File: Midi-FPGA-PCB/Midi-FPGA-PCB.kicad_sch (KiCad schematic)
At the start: 4 parts

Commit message: Arranged and documented
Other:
- title: (none) -> Midi FPGA
- moved on the sheet: H1, H2, H3, H4
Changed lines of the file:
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@@
 (kicad_sch (version 20230121) (generator eeschema)
   (paper "A4")
-  (rectangle (start 20.32 16.51) (end 72.39 45.72)
+  (title_block
+    (title "Midi FPGA")
+    (date "2023-11-07")
+    (rev "1.0")
+  )
+  (wire (pts (xy 20.32 22.86) (xy 20.32 24.13))
+    (stroke (width 0) (type default))
+  )
+  (wire (pts (xy 45.72 38.1) (xy 45.72 36.83))
+    (stroke (width 0) (type default))
+  )
+  (wire (pts (xy 20.32 38.1) (xy 20.32 36.83))
+    (stroke (width 0) (type default))
+  )
+  (wire (pts (xy 45.72 22.86) (xy 45.72 24.13))
+    (stroke (width 0) (type default))
+  )
+  (rectangle (start 15.24 15.24) (end 67.31 44.45)
     (stroke (width 0) (type default))
     (fill (type none))
   )
-  (symbol (lib_id "Mechanical:MountingHole_Pad") (at 50.8 35.56 0) (unit 1)
+  (symbol (lib_id "Mechanical:MountingHole_Pad") (at 45.72 34.29 0) (unit 1)
     (in_bom yes) (on_board yes) (dnp no) (fields_autoplaced)
-    (property "Reference" "H4" (at 53.34 33.02 0)
+    (property "Reference" "H4" (at 48.26 31.75 0)
       (effects (font (size 1.27 1.27)) (justify left))
     )
-    (property "Value" "MountingHole_Pad" (at 53.34 35.56 0)
+    (property "Value" "MountingHole_Pad" (at 48.26 34.29 0)
       (effects (font (size 1.27 1.27)) (justify left))
     )
-    (property "Footprint" "MountingHole:MountingHole_2.2mm_M2_DIN965_Pad" (at 50.8 35.56 0)
+    (property "Footprint" "MountingHole:MountingHole_2.2mm_M2_DIN965_Pad" (at 45.72 34.29 0)
       (effects (font (size 1.27 1.27)) hide)
     )
-    (property "Datasheet" "~" (at 50.8 35.56 0)
+    (property "Datasheet" "~" (at 45.72 34.29 0)
       (effects (font (size 1.27 1.27)) hide)
     )
@@
     )
   )
-  (symbol (lib_id "Mechanical:MountingHole_Pad") (at 50.8 22.86 0) (unit 1)
+  (symbol (lib_id "Mechanical:MountingHole_Pad") (at 45.72 20.32 0) (unit 1)
     (in_bom yes) (on_board yes) (dnp no) (fields_autoplaced)
-    (property "Reference" "H2" (at 53.34 20.32 0)
+    (property "Reference" "H2" (at 48.26 17.78 0)
       (effects (font (size 1.27 1.27)) (justify left))
     )
-    (property "Value" "MountingHole_Pad" (at 53.34 22.86 0)
+    (property "Value" "MountingHole_Pad" (at 48.26 20.32 0)
       (effects (font (size 1.27 1.27)) (justify left))
     )
-    (property "Footprint" "MountingHole:MountingHole_2.2mm_M2_DIN965_Pad" (at 50.8 22.86 0)
+    (property "Footprint" "MountingHole:MountingHole_2.2mm_M2_DIN965_Pad" (at 45.72 20.32 0)
       (effects (font (size 1.27 1.27)) hide)
     )
-    (property "Datasheet" "~" (at 50.8 22.86 0)
+    (property "Datasheet" "~" (at 45.72 20.32 0)
       (effects (font (size 1.27 1.27)) hide)
     )
@@
     )
   )
-  (symbol (lib_id "power:GND") (at 50.8 38.1 0) (unit 1)
+  (symbol (lib_id "power:GND") (at 45.72 38.1 0) (unit 1)
     (in_bom yes) (on_board yes) (dnp no) (fields_autoplaced)
-    (property "Reference" "#PWR04" (at 50.8 44.45 0)
+    (property "Reference" "#PWR04" (at 45.72 44.45 0)
       (effects (font (size 1.27 1.27)) hide)
     )
-    (property "Value" "GND" (at 50.8 43.18 0)
+    (property "Value" "GND" (at 45.72 43.18 0)
       (effects (font (size 1.27 1.27)))
     )
-    (property "Footprint" "" (at 50.8 38.1 0)
+    (property "Footprint" "" (at 45.72 38.1 0)
       (effects (font (size 1.27 1.27)) hide)
     )
-    (property "Datasheet" "" (at 50.8 38.1 0)
+    (property "Datasheet" "" (at 45.72 38.1 0)
       (effects (font (size 1.27 1.27)) hide)
     )
@@
     )
   )
-  (symbol (lib_id "power:GND") (at 50.8 25.4 0) (unit 1)
+  (symbol (lib_id "power:GND") (at 45.72 24.13 0) (unit 1)
     (in_bom yes) (on_board yes) (dnp no) (fields_autoplaced)
-    (property "Reference" "#PWR02" (at 50.8 31.75 0)
+    (property "Reference" "#PWR02" (at 45.72 30.48 0)
       (effects (font (size 1.27 1.27)) hide)
     )
-    (property "Value" "GND" (at 50.8 30.48 0)
+    (property "Value" "GND" (at 45.72 29.21 0)
       (effects (font (size 1.27 1.27)))
     )
-    (property "Footprint" "" (at 50.8 25.4 0)
+    (property "Footprint" "" (at 45.72 24.13 0)
       (effects (font (size 1.27 1.27)) hide)
     )
-    (property "Datasheet" "" (at 50.8 25.4 0)
+    (property "Datasheet" "" (at 45.72 24.13 0)
       (effects (font (size 1.27 1.27)) hide)
     )
@@
     )
   )
-  (symbol (lib_id "Mechanical:MountingHole_Pad") (at 25.4 22.86 0) (unit 1)
+  (symbol (lib_id "Mechanical:MountingHole_Pad") (at 20.32 20.32 0) (unit 1)
     (in_bom yes) (on_board yes) (dnp no) (fields_autoplaced)
-    (property "Reference" "H1" (at 27.94 20.32 0)
+    (property "Reference" "H1" (at 22.86 17.78 0)
       (effects (font (size 1.27 1.27)) (justify left))
     )
-    (property "Value" "MountingHole_Pad" (at 27.94 22.86 0)
+    (property "Value" "MountingHole_Pad" (at 22.86 20.32 0)
       (effects (font (size 1.27 1.27)) (justify left))
     )
-    (property "Footprint" "MountingHole:MountingHole_2.2mm_M2_DIN965_Pad" (at 25.4 22.86 0)
+    (property "Footprint" "MountingHole:MountingHole_2.2mm_M2_DIN965_Pad" (at 20.32 20.32 0)
       (effects (font (size 1.27 1.27)) hide)
     )
-    (property "Datasheet" "~" (at 25.4 22.86 0)
+    (property "Datasheet" "~" (at 20.32 20.32 0)
       (effects (font (size 1.27 1.27)) hide)
     )
@@
     )
   )
-  (symbol (lib_id "power:GND") (at 25.4 25.4 0) (unit 1)
+  (symbol (lib_id "power:GND") (at 20.32 24.13 0) (unit 1)
     (in_bom yes) (on_board yes) (dnp no) (fields_autoplaced)
-    (property "Reference" "#PWR01" (at 25.4 31.75 0)
+    (property "Reference" "#PWR01" (at 20.32 30.48 0)
       (effects (font (size 1.27 1.27)) hide)
     )
-    (property "Value" "GND" (at 25.4 30.48 0)
+    (property "Value" "GND" (at 20.32 29.21 0)
       (effects (font (size 1.27 1.27)))
     )
-    (property "Footprint" "" (at 25.4 25.4 0)
+    (property "Footprint" "" (at 20.32 24.13 0)
       (effects (font (size 1.27 1.27)) hide)
     )
-    (property "Datasheet" "" (at 25.4 25.4 0)
+    (property "Datasheet" "" (at 20.32 24.13 0)
       (effects (font (size 1.27 1.27)) hide)
     )
@@
     )
   )
-  (symbol (lib_id "Mechanical:MountingHole_Pad") (at 25.4 35.56 0) (unit 1)
+  (symbol (lib_id "Mechanical:MountingHole_Pad") (at 20.32 34.29 0) (unit 1)
     (in_bom yes) (on_board yes) (dnp no) (fields_autoplaced)
-    (property "Reference" "H3" (at 27.94 33.02 0)
+    (property "Reference" "H3" (at 22.86 31.75 0)
       (effects (font (size 1.27 1.27)) (justify left))
     )
-    (property "Value" "MountingHole_Pad" (at 27.94 35.56 0)
+    (property "Value" "MountingHole_Pad" (at 22.86 34.29 0)
       (effects (font (size 1.27 1.27)) (justify left))
     )
-    (property "Footprint" "MountingHole:MountingHole_2.2mm_M2_DIN965_Pad" (at 25.4 35.56 0)
+    (property "Footprint" "MountingHole:MountingHole_2.2mm_M2_DIN965_Pad" (at 20.32 34.29 0)
       (effects (font (size 1.27 1.27)) hide)
     )
-    (property "Datasheet" "~" (at 25.4 35.56 0)
+    (property "Datasheet" "~" (at 20.32 34.29 0)
       (effects (font (size 1.27 1.27)) hide)
     )
@@
     )
   )
-  (symbol (lib_id "power:GND") (at 25.4 38.1 0) (unit 1)
+  (symbol (lib_id "power:GND") (at 20.32 38.1 0) (unit 1)
     (in_bom yes) (on_board yes) (dnp no) (fields_autoplaced)
-    (property "Reference" "#PWR03" (at 25.4 44.45 0)
+    (property "Reference" "#PWR03" (at 20.32 44.45 0)
       (effects (font (size 1.27 1.27)) hide)
     )
-    (property "Value" "GND" (at 25.4 43.18 0)
+    (property "Value" "GND" (at 20.32 43.18 0)
       (effects (font (size 1.27 1.27)))
     )
-    (property "Footprint" "" (at 25.4 38.1 0)
+    (property "Footprint" "" (at 20.32 38.1 0)
       (effects (font (size 1.27 1.27)) hide)
     )
-    (property "Datasheet" "" (at 25.4 38.1 0)
+    (property "Datasheet" "" (at 20.32 38.1 0)
       (effects (font (size 1.27 1.27)) hide)
     )

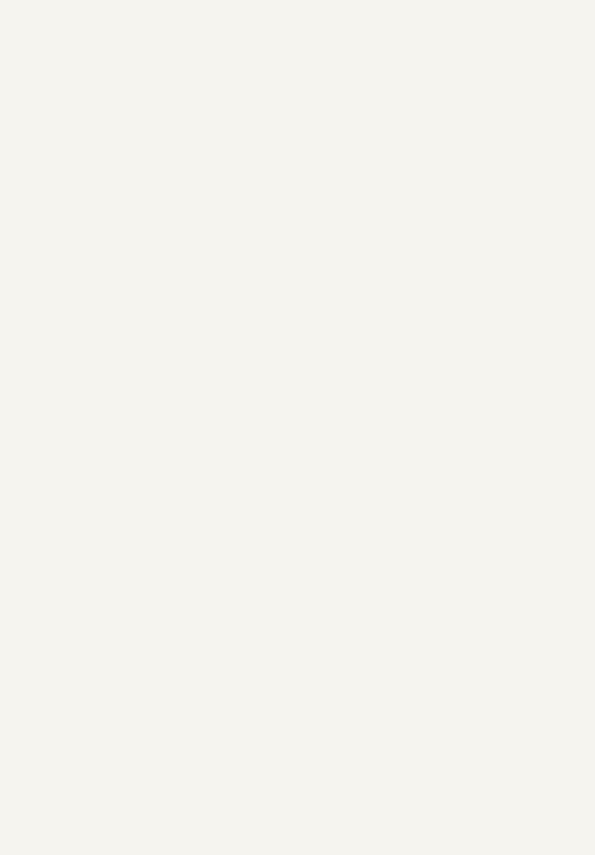
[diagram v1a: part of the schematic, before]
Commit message: Placed ESP32
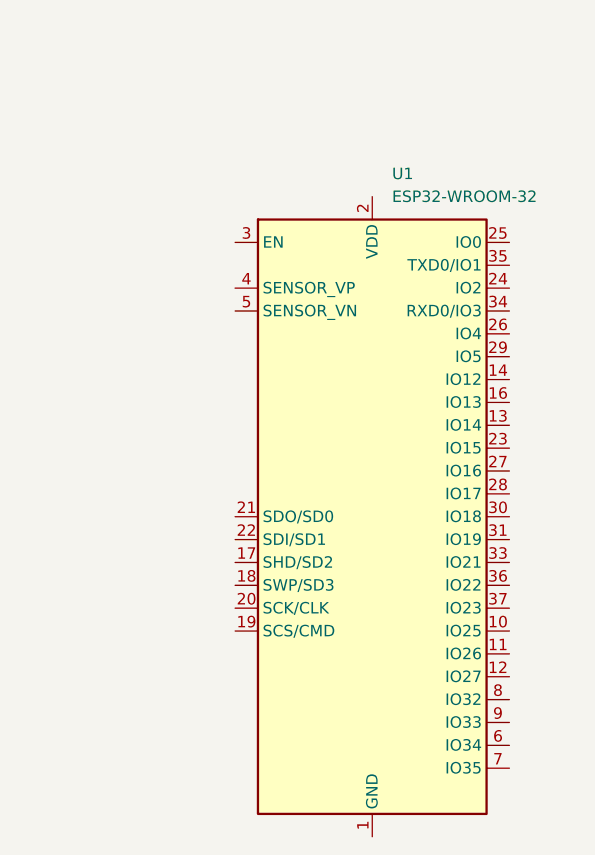
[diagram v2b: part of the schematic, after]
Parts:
- added U1: ESP32-WROOM-32, Midi-FPGA-lib:ESP32-WROOM-32 (No Thermal), symbol Midi-FGPA-lib:ESP32-WROOM-32_(No_Thermal)
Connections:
- new net: U1.1 (GND), U1.15 (GND), U1.38 (GND)
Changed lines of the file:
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@@
+    )
+  )
+  (symbol (lib_id "Midi-FGPA-lib:ESP32-WROOM-32_(No_Thermal)") (at 139.7 97.79 0) (unit 1)
+    (in_bom yes) (on_board yes) (dnp no) (fields_autoplaced)
+    (property "Reference" "U1" (at 141.8941 59.69 0)
+      (effects (font (size 1.27 1.27)) (justify left))
+    )
+    (property "Value" "ESP32-WROOM-32" (at 141.8941 62.23 0)
+      (effects (font (size 1.27 1.27)) (justify left))
+    )
+    (property "Footprint" "Midi-FPGA-lib:ESP32-WROOM-32 (No Thermal)" (at 139.7 135.89 0)
+      (effects (font (size 1.27 1.27)) hide)
+    )
+    (property "Datasheet" "https://www.espressif.com/sites/default/files/documentation/esp32-wroom-32e_esp32-wroom-32ue_datasheet_en.pdf" (at 132.08 96.52 0)
+      (effects (font (size 1.27 1.27)) hide)
+    )
+    (property "Store page" "https://www.digikey.co.uk/en/products/detail/espressif-systems/ESP32-WROOM-32E-N4/11613125" (at 139.7 97.79 0)
+      (effects (font (size 1.27 1.27)) hide)
+    )
+    (pin "1")
+    (pin "10")
+    (pin "11")
+    (pin "12")
+    (pin "13")
+    (pin "14")
+    (pin "15")
+    (pin "16")
+    (pin "17")
+    (pin "18")
+    (pin "19")
+    (pin "2")
+    (pin "20")
+    (pin "21")
+    (pin "22")
+    (pin "23")
+    (pin "24")
+    (pin "25")
+    (pin "26")
+    (pin "27")
+    (pin "28")
+    (pin "29")
+    (pin "3")
+    (pin "30")
+    (pin "31")
+    (pin "32")
+    (pin "33")
+    (pin "34")
+    (pin "35")
+    (pin "36")
+    (pin "37")
+    (pin "38")
+    (pin "4")
+    (pin "5")
+    (pin "6")
+    (pin "7")
+    (pin "8")
+    (pin "9")
+    (instances
+      (project "Midi-FPGA-PCB"
+        (path "/75ad38e9-b0d3-45bc-bcac-026c9800f4ea"
+          (reference "U1") (unit 1)
+        )
+      )
     )
   )

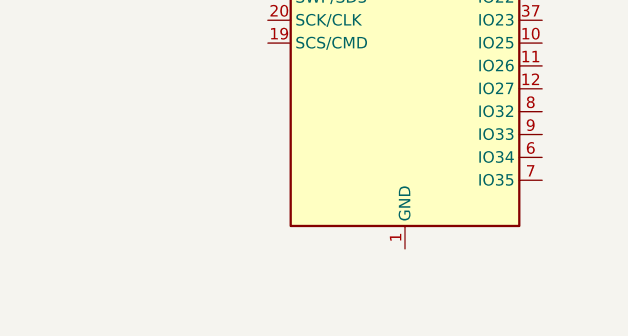
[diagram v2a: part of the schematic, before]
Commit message: Added ground fills
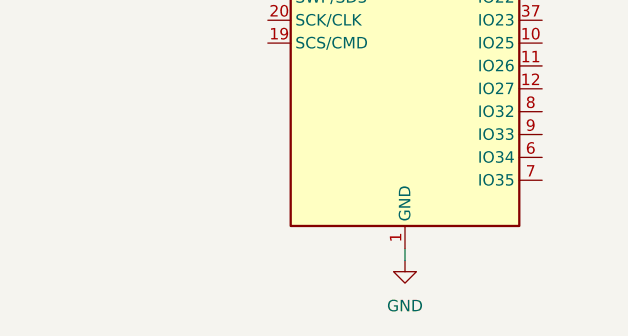
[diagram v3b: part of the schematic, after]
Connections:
- net GND: now also U1.1 (GND), U1.15 (GND), U1.38 (GND)
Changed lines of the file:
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@@
+    (stroke (width 0) (type default))
+  )
+  (wire (pts (xy 139.7 133.35) (xy 139.7 134.62))
     (stroke (width 0) (type default))
   )
@@
         )
       )
+    )
+  )
+  (symbol (lib_id "power:GND") (at 139.7 134.62 0) (unit 1)
+    (in_bom yes) (on_board yes) (dnp no) (fields_autoplaced)
+    (property "Reference" "#PWR05" (at 139.7 140.97 0)
+      (effects (font (size 1.27 1.27)) hide)
+    )
+    (property "Value" "GND" (at 139.7 139.7 0)
+      (effects (font (size 1.27 1.27)))
+    )
+    (property "Footprint" "" (at 139.7 134.62 0)
+      (effects (font (size 1.27 1.27)) hide)
+    )
+    (property "Datasheet" "" (at 139.7 134.62 0)
+      (effects (font (size 1.27 1.27)) hide)
+    )
+    (pin "1")
+    (instances
+      (project "Midi-FPGA-PCB"
+        (path "/75ad38e9-b0d3-45bc-bcac-026c9800f4ea"
+          (reference "#PWR05") (unit 1)
+        )
+      )
